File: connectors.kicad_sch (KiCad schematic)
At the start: 4 parts, among them J1 Conn_01x04_Pin, J2 Conn_01x04_Pin, J3 Conn_01x09_Pin, J4 Conn_02x03_Odd_Even

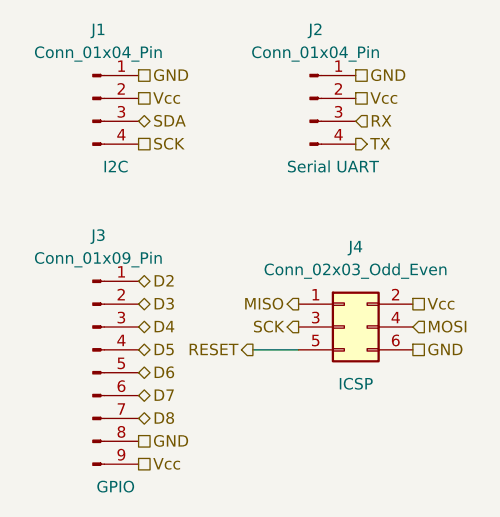
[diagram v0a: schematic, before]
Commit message: Fixed two defects in the schematic.
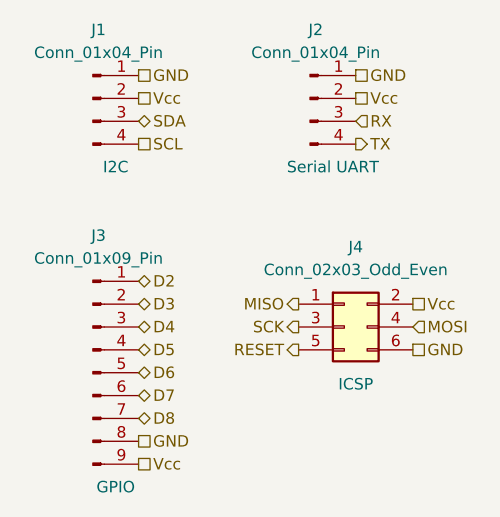
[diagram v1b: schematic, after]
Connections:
- net SCK: no longer J1.4 (Pin_4)
- new net SCL: J1.4 (Pin_4)
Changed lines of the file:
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@@
 (kicad_sch (version 20230121) (generator eeschema)
   (paper "A4")
-  (wire (pts (xy 204.47 107.95) (xy 199.39 107.95))
-    (stroke (width 0) (type default))
-  )
   (hierarchical_label "GND" (shape passive) (at 210.82 77.47 0) (fields_autoplaced)
     (effects (font (size 1.27 1.27)) (justify left))
@@
     (effects (font (size 1.27 1.27)) (justify left))
   )
-  (hierarchical_label "RESET" (shape output) (at 199.39 107.95 180) (fields_autoplaced)
+  (hierarchical_label "RESET" (shape output) (at 204.47 107.95 180) (fields_autoplaced)
     (effects (font (size 1.27 1.27)) (justify right))
   )
@@
     (effects (font (size 1.27 1.27)) (justify left))
   )
-  (hierarchical_label "SCK" (shape passive) (at 186.69 85.09 0) (fields_autoplaced)
+  (hierarchical_label "SCL" (shape passive) (at 186.69 85.09 0) (fields_autoplaced)
     (effects (font (size 1.27 1.27)) (justify left))
   )
